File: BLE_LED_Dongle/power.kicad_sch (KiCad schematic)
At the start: 22 parts, among them J3 USB_C_Receptacle_PowerOnly_6P, SW1 SW_SPDT, U2 TPS61023DRLR, U3 TP4056-42-ESOP8, U4 XC6206PxxxMR

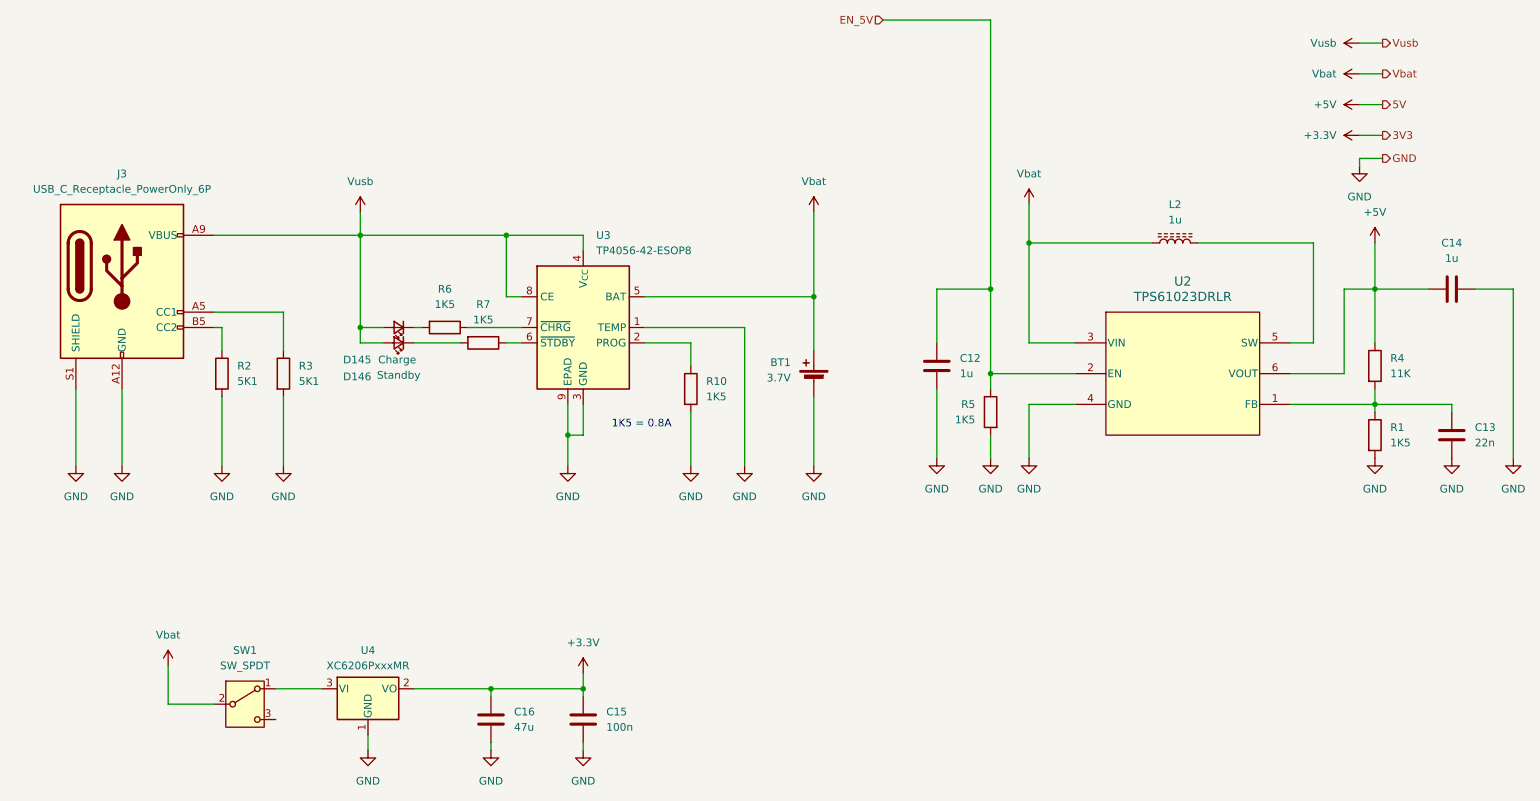
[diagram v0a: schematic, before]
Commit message: progress: PCB Part Placement of Patterns Complete
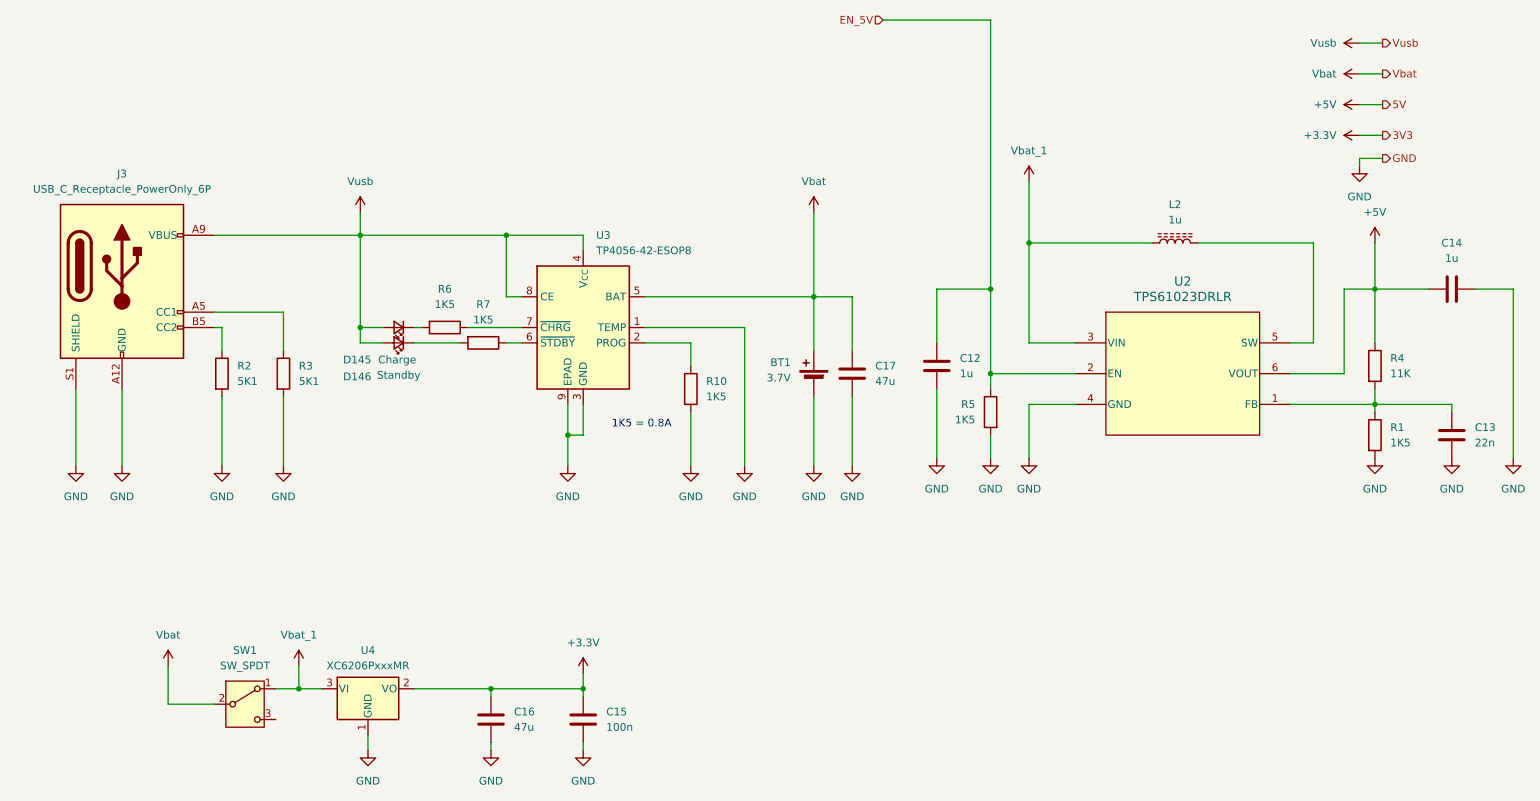
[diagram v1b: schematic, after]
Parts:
- added C17: 47u, Capacitor_SMD:C_1206_3216Metric, symbol Device:C
- C12, C13, C14, C15: footprint (none) -> Capacitor_SMD:C_0402_1005Metric
- C16: footprint (none) -> Capacitor_SMD:C_1206_3216Metric
- D145, D146: footprint (none) -> LED_SMD:LED_0603_1608Metric
- R1, R10, R2, R3, R4, R5, R6, R7: footprint (none) -> Resistor_SMD:R_0603_1608Metric
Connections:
- net GND: now also C17.1
- net Vbat: now also C17.2; no longer L2.1, U2.3 (VIN)
- net Vbat_1: now reaches SW1.1 (A), U4.3 (VI)
- net Vbat_1: now also L2.1, U2.3 (VIN)

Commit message: progress: board 1 complete, board 2 schematics in progress.
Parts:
- BT1: LCSC (none) -> C295747
- C12, C14: LCSC (none) -> C14445
- C13: LCSC (none) -> C337699
- C15: LCSC (none) -> C1525
- C16, C17: LCSC (none) -> C68361
- D145: LCSC (none) -> C19171390
- D146: LCSC (none) -> C22371297
- J3: LCSC (none) -> C668623
- L2: LCSC (none) -> C5343973
- R1, R10, R5, R6, R7: LCSC (none) -> C22843
- R2, R3: LCSC (none) -> C23186
- R4: LCSC (none) -> C2906986
- SW1: LCSC (none) -> C431547
- U2: LCSC (none) -> C919459
- U3: LCSC (none) -> C382139
- U4: LCSC (none) -> C5446
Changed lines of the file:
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@@
 			)
 		)
+		(property "LCSC" "C2906986"
+			(at 246.38 83.82 0)
+			(effects
+				(font
+					(size 1.27 1.27)
+				)
+				(hide yes)
+			)
+		)
 		(pin "1"
 		)
@@
 			)
 		)
+		(property "LCSC" "C22371297"
+			(at 85.09 80.01 0)
+			(effects
+				(font
+					(size 1.27 1.27)
+				)
+				(hide yes)
+			)
+		)
 		(pin "2"
 		)
@@
 			)
 		)
+		(property "LCSC" "C23186"
+			(at 66.04 85.09 0)
+			(effects
+				(font
+					(size 1.27 1.27)
+				)
+				(hide yes)
+			)
+		)
 		(pin "2"
 		)
@@
 			)
 		)
+		(property "LCSC" "C1525"
+			(at 115.57 142.24 0)
+			(effects
+				(font
+					(size 1.27 1.27)
+				)
+				(hide yes)
+			)
+		)
 		(pin "2"
 		)
@@
 			)
 		)
+		(property "LCSC" "C22843"
+			(at 246.38 95.25 0)
+			(effects
+				(font
+					(size 1.27 1.27)
+				)
+				(hide yes)
+			)
+		)
 		(pin "1"
 		)
@@
 			)
 		)
+		(property "LCSC" "C337699"
+			(at 259.08 95.25 0)
+			(effects
+				(font
+					(size 1.27 1.27)
+				)
+				(hide yes)
+			)
+		)
 		(pin "2"
 		)
@@
 			)
 		)
+		(property "LCSC" "C295747"
+			(at 153.67 86.36 0)
+			(effects
+				(font
+					(size 1.27 1.27)
+				)
+				(hide yes)
+			)
+		)
 		(pin "1"
 		)
@@
 			)
 		)
+		(property "LCSC" "C14445"
+			(at 173.99 83.82 0)
+			(effects
+				(font
+					(size 1.27 1.27)
+				)
+				(hide yes)
+			)
+		)
 		(pin "2"
 		)
@@
 			)
 		)
+		(property "LCSC" "C22843"
+			(at 182.88 91.44 0)
+			(effects
+				(font
+					(size 1.27 1.27)
+				)
+				(hide yes)
+			)
+		)
 		(pin "2"
 		)
@@
 			)
 		)
+		(property "LCSC" "C68361"
+			(at 160.02 85.09 0)
+			(effects
+				(font
+					(size 1.27 1.27)
+				)
+				(hide yes)
+			)
+		)
 		(pin "2"
 		)
@@
 			)
 		)
+		(property "LCSC" "C23186"
+			(at 55.88 85.09 0)
+			(effects
+				(font
+					(size 1.27 1.27)
+				)
+				(hide yes)
+			)
+		)
 		(pin "2"
 		)
@@
 			)
 		)
+		(property "LCSC" "C668623"
+			(at 39.37 69.85 0)
+			(effects
+				(font
+					(size 1.27 1.27)
+				)
+				(hide yes)
+			)
+		)
 		(pin "S1"
 		)
@@
 			)
 		)
+		(property "LCSC" "C68361"
+			(at 100.33 142.24 0)
+			(effects
+				(font
+					(size 1.27 1.27)
+				)
+				(hide yes)
+			)
+		)
 		(pin "2"
 		)
@@
 			)
 		)
+		(property "LCSC" "C431547"
+			(at 59.69 139.7 0)
+			(effects
+				(font
+					(size 1.27 1.27)
+				)
+				(hide yes)
+			)
+		)
 		(pin "1"
 		)
@@
 			)
 		)
+		(property "LCSC" "C19171390"
+			(at 85.09 77.47 0)
+			(effects
+				(font
+					(size 1.27 1.27)
+				)
+				(hide yes)
+			)
+		)
 		(pin "1"
 		)
@@
 			)
 		)
+		(property "LCSC" "C22843"
+			(at 133.35 87.63 0)
+			(effects
+				(font
+					(size 1.27 1.27)
+				)
+				(hide yes)
+			)
+		)
 		(pin "2"
 		)
@@
 			)
 		)
+		(property "LCSC" "C5343973"
+			(at 213.36 63.5 90)
+			(effects
+				(font
+					(size 1.27 1.27)
+				)
+				(hide yes)
+			)
+		)
 		(pin "1"
 		)
@@
 			)
 		)
+		(property "LCSC" "C919459"
+			(at 214.63 85.09 0)
+			(effects
+				(font
+					(size 1.27 1.27)
+				)
+				(hide yes)
+			)
+		)
 		(pin "3"
 		)
@@
 			)
 		)
+		(property "LCSC" "C14445"
+			(at 259.08 71.12 90)
+			(effects
+				(font
+					(size 1.27 1.27)
+				)
+				(hide yes)
+			)
+		)
 		(pin "2"
 		)
@@
 			)
 		)
+		(property "LCSC" "C382139"
+			(at 115.57 77.47 0)
+			(effects
+				(font
+					(size 1.27 1.27)
+				)
+				(hide yes)
+			)
+		)
 		(pin "4"
 		)
@@
 			)
 		)
+		(property "LCSC" "C22843"
+			(at 92.71 77.47 90)
+			(effects
+				(font
+					(size 1.27 1.27)
+				)
+				(hide yes)
+			)
+		)
 		(pin "2"
 		)
@@
 			)
 		)
+		(property "LCSC" "C22843"
+			(at 99.06 80.01 90)
+			(effects
+				(font
+					(size 1.27 1.27)
+				)
+				(hide yes)
+			)
+		)
 		(pin "2"
 		)
@@
 			(at 80.01 137.16 0)
 			(effects
+				(font
+					(size 1.27 1.27)
+				)
+				(hide yes)
+			)
+		)
+		(property "LCSC" "C5446"
+			(at 80.01 137.16 0)
+			(effects
